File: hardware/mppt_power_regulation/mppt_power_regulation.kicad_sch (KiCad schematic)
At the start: 74 parts, among them IC101 LMR38010SDDAR, IC102 TPS2121, J101 CT3151, J102 CT3151, J103 CT3151, J104 CT3151, J105 CT3151, J106 CT3151, J107 CT3151, J108 CT3151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

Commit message: gave names to unlabeled nets
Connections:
- net 12MUXLED: now reaches D104.2 (A), R112.2
- net 5to3V3LED: now reaches D106.2 (A), R115.2
- net 12to5LED: now reaches D101.2 (A), R103.2
- net 5VISO_RAW: now reaches L103.1, PS101.8 (+VOUT)
- net +V_ARR: now reaches C103.1, C104.1, C106.1, IC101.3 (VIN), J101.1, J101.2 (1), J101.3 (1), J101.4 (1), R119.1, TP102.1
- net EN_inner: now reaches R119.2, R120.1
- net CP2: now reaches IC102.3 (CP2), R114.2, R117.1
- net ILIM: now reaches IC102.10 (ILIM), R118.1
- net SS: now reaches C117.1, IC102.11 (SS)
- net PR1: now reaches IC102.6 (PR1), R109.2, R111.1
- net 5VISO_LED: now reaches D102.2 (A), R107.2
- net EN_VINto12: now reaches IC101.2 (EN), R120.2, R121.1
- net RT/Sync: now reaches IC101.4 (RT/SYNC), R105.1
- net FB_VINto12: now reaches IC101.5 (FB), R104.2, R106.1
- net BOOT_VINto12: now reaches C101.1, IC101.7 (BOOT)
- net SW_VINto12: now reaches C101.2, IC101.8 (SW), L101.1
- net SW_12to5: now reaches C102.2, L102.1, U101.5 (SW)
- net FB_inner: now reaches R101.2, R104.1
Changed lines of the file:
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@@
+	(wire
+		(pts
+			(xy 106.68 36.83) (xy 109.22 36.83)
+		)
+		(stroke
+			(width 0)
+			(type default)
+		)
+	)
 	(wire
 		(pts
@@
 		(pts
 			(xy 134.62 143.51) (xy 144.78 143.51)
-		)
-		(stroke
-			(width 0)
-			(type default)
-		)
-	)
-	(wire
-		(pts
-			(xy 106.68 36.83) (xy 109.22 36.83)
 		)
 		(stroke
@@
 		)
 	)
+	(label "12MUXLED"
+		(at 144.78 125.73 0)
+		(fields_autoplaced yes)
+		(effects
+			(font
+				(size 1.27 1.27)
+			)
+			(justify left bottom)
+		)
+	)
 	(label "OV2"
 		(at 58.42 129.54 180)
@@
 		)
 	)
+	(label "CP2"
+		(at 80.01 129.54 0)
+		(fields_autoplaced yes)
+		(effects
+			(font
+				(size 1.27 1.27)
+			)
+			(justify left bottom)
+		)
+	)
+	(label "SS"
+		(at 115.57 124.46 0)
+		(fields_autoplaced yes)
+		(effects
+			(font
+				(size 1.27 1.27)
+			)
+			(justify left bottom)
+		)
+	)
+	(label "SW_12to5"
+		(at 213.36 35.56 90)
+		(fields_autoplaced yes)
+		(effects
+			(font
+				(size 1.27 1.27)
+			)
+			(justify left bottom)
+		)
+	)
+	(label "5to3V3LED"
+		(at 218.44 132.08 0)
+		(fields_autoplaced yes)
+		(effects
+			(font
+				(size 1.27 1.27)
+			)
+			(justify left bottom)
+		)
+	)
+	(label "ILIM"
+		(at 115.57 129.54 0)
+		(fields_autoplaced yes)
+		(effects
+			(font
+				(size 1.27 1.27)
+			)
+			(justify left bottom)
+		)
+	)
 	(label "PG"
 		(at 53.34 25.4 0)
@@
 		)
 	)
+	(label "5VISO_RAW"
+		(at 223.52 80.01 90)
+		(fields_autoplaced yes)
+		(effects
+			(font
+				(size 1.27 1.27)
+			)
+			(justify left bottom)
+		)
+	)
+	(label "+V_ARR"
+		(at 44.45 36.83 0)
+		(fields_autoplaced yes)
+		(effects
+			(font
+				(size 1.27 1.27)
+			)
+			(justify left bottom)
+		)
+	)
+	(label "RT{slash}Sync"
+		(at 69.85 44.45 270)
+		(fields_autoplaced yes)
+		(effects
+			(font
+				(size 1.27 1.27)
+			)
+			(justify right bottom)
+		)
+	)
+	(label "FB_VINto12"
+		(at 107.95 46.99 0)
+		(fields_autoplaced yes)
+		(effects
+			(font
+				(size 1.27 1.27)
+			)
+			(justify left bottom)
+		)
+	)
+	(label "12to5LED"
+		(at 243.84 45.72 0)
+		(fields_autoplaced yes)
+		(effects
+			(font
+				(size 1.27 1.27)
+			)
+			(justify left bottom)
+		)
+	)
 	(label "PG"
 		(at 107.95 44.45 0)
@@
 		)
 	)
+	(label "EN_VINto12"
+		(at 67.31 39.37 90)
+		(fields_autoplaced yes)
+		(effects
+			(font
+				(size 1.27 1.27)
+			)
+			(justify left bottom)
+		)
+	)
+	(label "EN_inner"
+		(at 57.15 43.18 90)
+		(fields_autoplaced yes)
+		(effects
+			(font
+				(size 1.27 1.27)
+			)
+			(justify left bottom)
+		)
+	)
+	(label "FB_inner"
+		(at 134.62 41.91 90)
+		(fields_autoplaced yes)
+		(effects
+			(font
+				(size 1.27 1.27)
+			)
+			(justify left bottom)
+		)
+	)
+	(label "FB_12to5"
+		(at 222.25 35.56 90)
+		(fields_autoplaced yes)
+		(effects
+			(font
+				(size 1.27 1.27)
+			)
+			(justify left bottom)
+		)
+	)
+	(label "BOOT_VINto12"
+		(at 107.95 36.83 90)
+		(fields_autoplaced yes)
+		(effects
+			(font
+				(size 1.27 1.27)
+			)
+			(justify left bottom)
+		)
+	)
 	(label "OV1"
 		(at 58.42 111.76 180)
@@
 		)
 	)
+	(label "PR1"
+		(at 80.01 111.76 0)
+		(fields_autoplaced yes)
+		(effects
+			(font
+				(size 1.27 1.27)
+			)
+			(justify left bottom)
+		)
+	)
+	(label "SW_VINto12"
+		(at 116.84 36.83 90)
+		(fields_autoplaced yes)
+		(effects
+			(font
+				(size 1.27 1.27)
+			)
+			(justify left bottom)
+		)
+	)
 	(label "OV2"
 		(at 83.82 135.89 180)
@@
 		)
 	)
+	(label "5VISO_LED"
+		(at 246.38 90.17 0)
+		(fields_autoplaced yes)
+		(effects
+			(font
+				(size 1.27 1.27)
+			)
+			(justify left bottom)
+		)
+	)

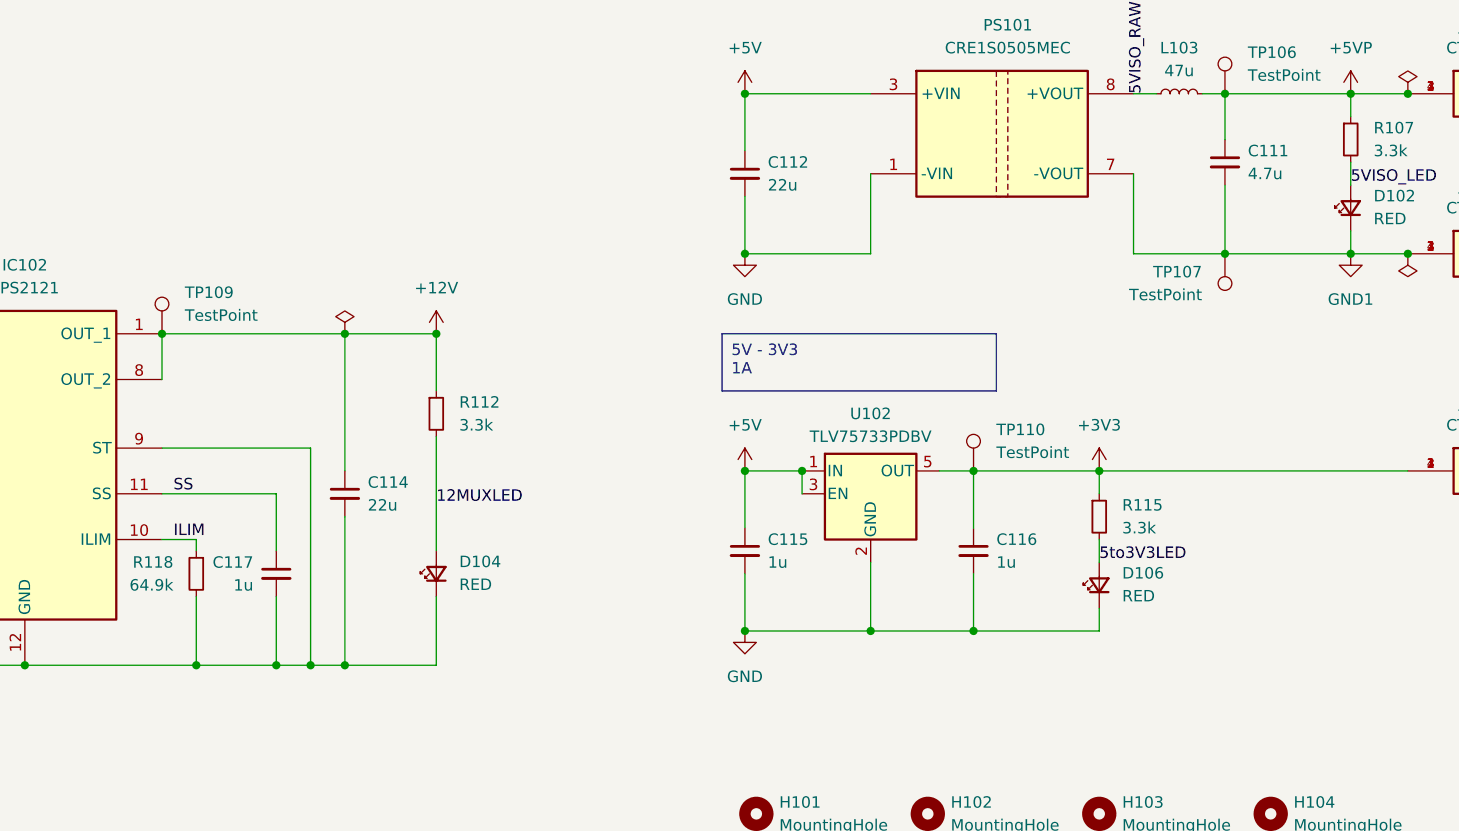
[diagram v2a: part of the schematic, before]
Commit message: update bom to remove lcsc dependency
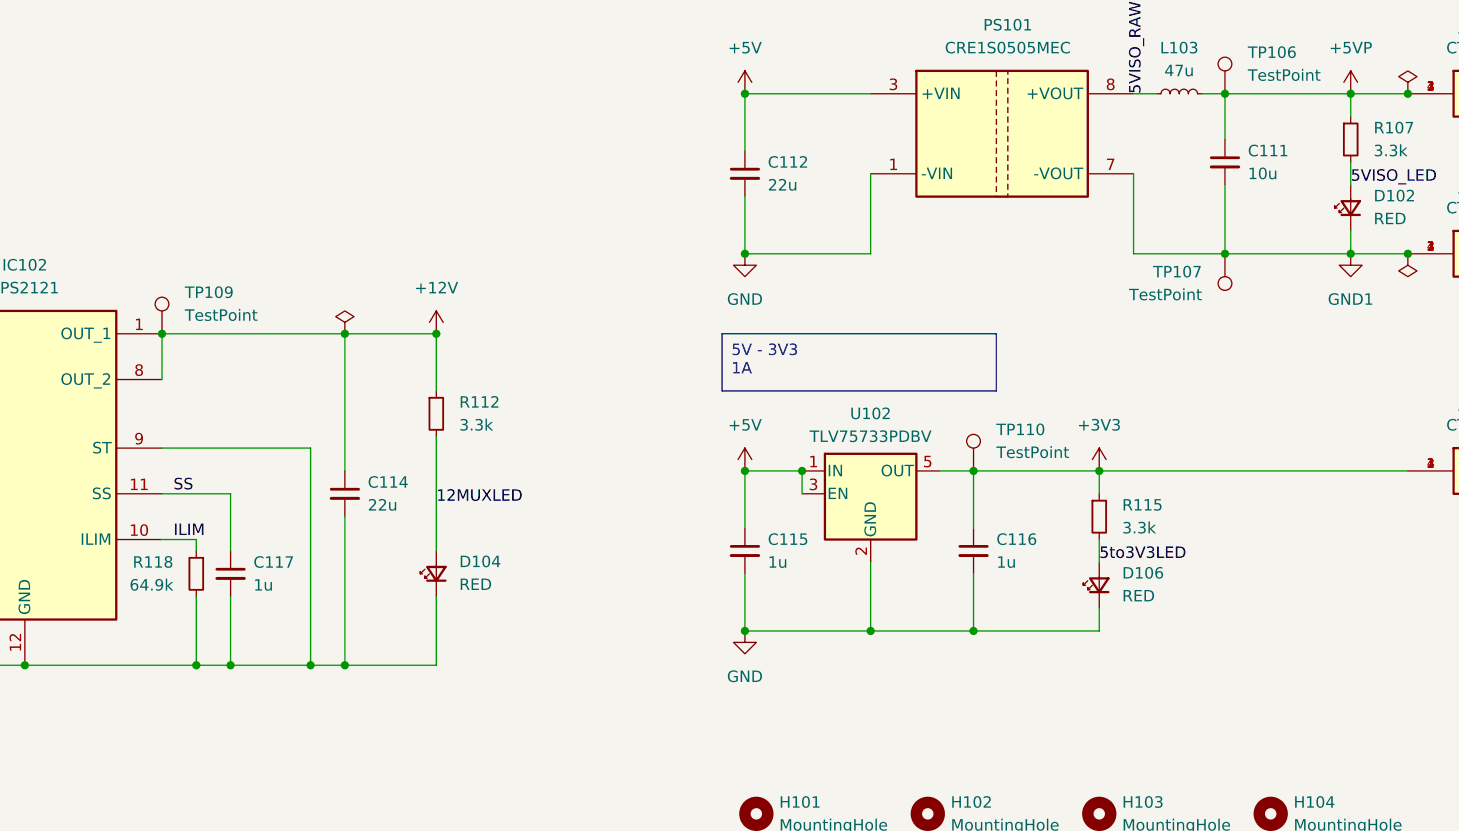
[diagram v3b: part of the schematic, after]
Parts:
- C101, C102, C106: Cost 0.0062 -> (none); Distributor LCSC -> (none); LCSC Part # C28233 -> (none)
- C103, C104: Cost 0.0764 -> (none); Distributor LCSC -> (none); LCSC Part # C170101 -> (none)
- C107, C109, C110, C112, C114: Cost 0.0215 -> (none); Distributor LCSC -> (none); LCSC Part # C45783 -> (none); P/N CL21A226MAQNNNE -> CL21A226MOCLRNC
- C108: Cost 0.0096 -> (none); Distributor LCSC -> (none); LCSC Part # C15850 -> (none); P/N CL21A106KAYNNNE -> CL21B106KOQNNNE
- C111: value 4.7u -> 10u; Cost 0.0230 -> (none); Distributor LCSC -> (none); LCSC Part # C98195 -> (none); P/N CL21B475KAFNNNE -> CL21B106KOQNNNE
- C113, C115, C116, C117, C118: Cost 0.0082 -> (none); Distributor LCSC -> (none); LCSC Part # C28323 -> (none); P/N CL21B105KBFNNNE -> CL21B105KAFVPNE
- D101, D102, D104, D106: Cost 0.0119 -> (none); Distributor LCSC -> (none); LCSC Part # C84256 -> (none); Manufacturer Foshan NationStar Optoelectronics -> Harvatek Corporation; Notes Harvatek B1701URO-20D000114U1930 for normal run -> (none); P/N NCD0805R1 -> B1701URO-20D000114U1930
- D103, D105: Cost 0.0950 -> (none); Distributor LCSC -> (none); LCSC Part # C223985 -> (none)
- IC101: Cost 2.054 -> (none)
- IC102: Cost 0.9435 -> (none); Distributor LCSC -> Texas Instruments; LCSC Part # C485916 -> (none); Notes TI for normal run -> (none)
- J101, J102, J103, J104, J105, J106, J107, J108: Cost 2.45 -> (none); Distributor Digikey -> (none)
- L101: Cost 0.2427 -> (none); Distributor Digikey -> (none); LCSC Part # C1330786 -> (none); Notes Digikey/Mouser for normal run -> (none)
- L102: Cost 0.2931 -> (none); Distributor Digikey -> (none); LCSC Part # C2044594 -> (none); Notes Digikey/Mouser for normal run -> (none)
- L103: Cost 0.2673 -> (none); Distributor Digikey -> (none); LCSC Part # C5151734 -> (none); Notes Digikey/Mouser for normal run -> (none)
- PS101: Cost 4.40 -> (none); Distributor Digikey -> (none)
- R101, R102, R108, R109, R113, R114, R119: Cost 0.0017 -> (none); Distributor LCSC -> (none); LCSC Part # C149504 -> (none); Manufacturer UNI-ROYAL(Uniroyal Elec) -> Vishay Dale; P/N 0805W8F1003T5E -> CRCW0805100KFKEA
- R103, R107, R112, R115: Cost 0.0017 -> (none); Distributor LCSC -> (none); LCSC Part # C26010 -> (none); Manufacturer UNI-ROYAL(Uniroyal Elec) -> Vishay Dale; P/N 0805W8F3301T5E -> CRCW08053K30FKEA
- R104, R106, R120, R121: Cost 0.0016 -> (none); Distributor LCSC -> (none); LCSC Part # C17414 -> (none); Manufacturer UNI-ROYAL(Uniroyal Elec) -> Vishay Dale; P/N 0805W8F1002T5E -> CRCW080510K0FKEA
- R105, R118: Cost 0.0018 -> (none); Distributor LCSC -> (none); LCSC Part # C17788 -> (none); Manufacturer UNI-ROYAL(Uniroyal Elec) -> Vishay Dale; P/N 0805W8F6492T5E -> CRCW080564K9FKEA
- R110, R116: Cost 0.0011 -> (none); Distributor LCSC -> (none); LCSC Part # C30041 -> (none); Manufacturer UNI-ROYAL(Uniroyal Elec) -> Vishay Dale; P/N 0805W8F7681T5E -> CRCW08057K68FKEA
- R111: Cost 0.0016 -> (none); Distributor LCSC -> (none); LCSC Part # C19796 -> (none); Manufacturer UNI-ROYAL(Uniroyal Elec) -> Vishay Dale; P/N 0805W8F1742T5E -> CRCW080517K4FKEA
- R117: Cost 0.0016 -> (none); Distributor LCSC -> (none); LCSC Part # C17464 -> (none); Manufacturer UNI-ROYAL(Uniroyal Elec) -> Vishay Dale; P/N 0805W8J0143T5E -> CRCW080514K0FKEA
- TP101, TP102, TP103, TP104, TP105, TP106, TP107, TP108, TP109, TP110: Cost 0.2627 -> (none); Distributor LCSC -> (none); LCSC Part # C5199900 -> (none); Notes Digikey/Mouser for normal run -> (none)
- U101: Cost 0.4380 -> (none); Distributor LCSC -> (none); LCSC Part # C2071056 -> (none); Notes Digikey/Mouser for normal run -> (none)
- U102: Cost 0.1677 -> (none); Distributor LCSC -> Texas Instruments; LCSC Part # C189779 -> (none); Notes Digikey/Mouser for normal run -> (none)
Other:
- moved on the sheet: C117
